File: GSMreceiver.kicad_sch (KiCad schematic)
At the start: 6 parts

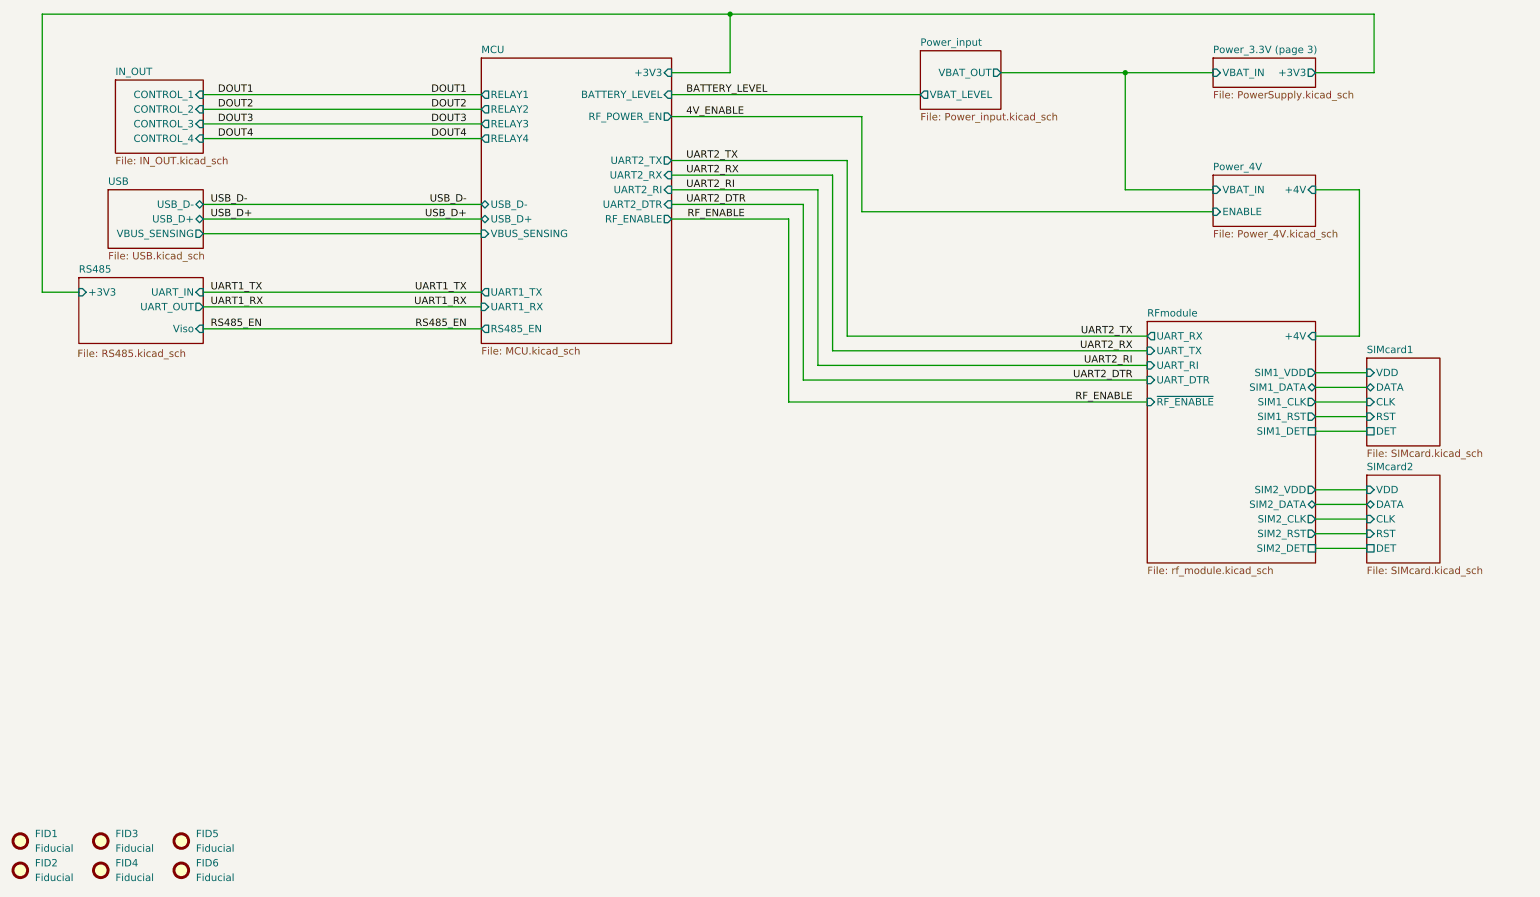
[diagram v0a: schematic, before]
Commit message: Replace SIM800C-DS with A7682E
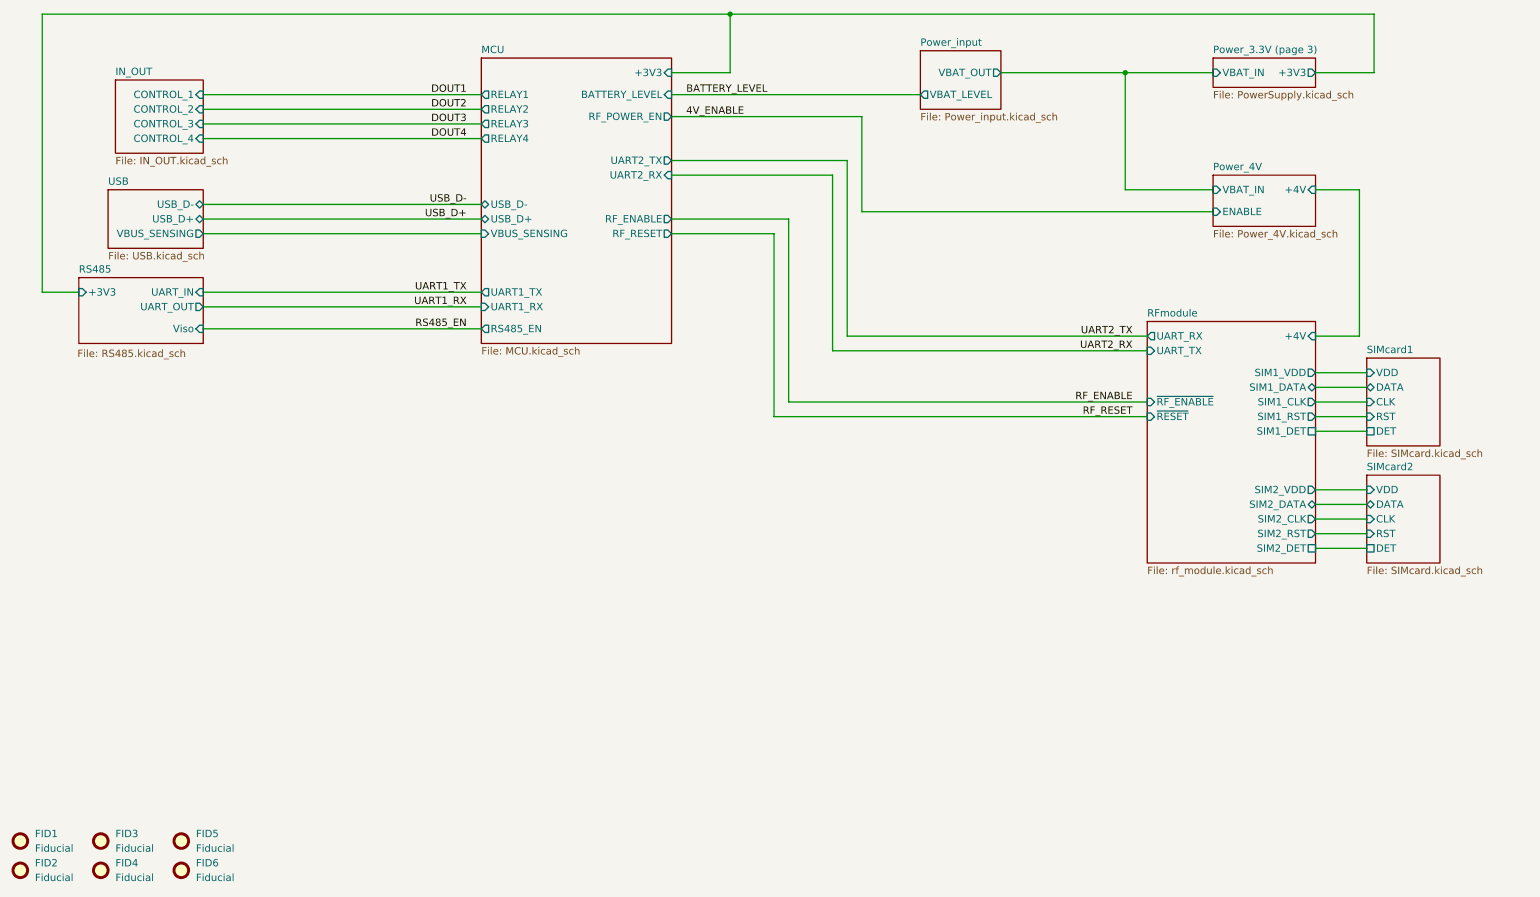
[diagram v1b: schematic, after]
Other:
- sheet MCU ports: added RF_RESET; removed UART2_DTR, UART2_RI
- sheet RFmodule ports: added ~{RESET}; removed UART_DTR, UART_RI
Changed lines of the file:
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@@
+	(wire
+		(pts
+			(xy 148.59 113.03) (xy 213.36 113.03)
+		)
+		(stroke
+			(width 0)
+			(type default)
+		)
+	)
 	(wire
 		(pts
@@
 	(wire
 		(pts
-			(xy 156.21 73.66) (xy 156.21 104.14)
-		)
-		(stroke
-			(width 0)
-			(type default)
-		)
-	)
-	(wire
-		(pts
 			(xy 49.53 59.69) (xy 97.79 59.69)
 		)
@@
 	(wire
 		(pts
+			(xy 130.81 81.28) (xy 148.59 81.28)
+		)
+		(stroke
+			(width 0)
+			(type default)
+		)
+	)
+	(wire
+		(pts
 			(xy 49.53 97.79) (xy 97.79 97.79)
 		)
@@
 	(wire
 		(pts
-			(xy 153.67 106.68) (xy 213.36 106.68)
-		)
-		(stroke
-			(width 0)
-			(type default)
-		)
-	)
-	(wire
-		(pts
 			(xy 224.79 73.66) (xy 209.55 73.66)
 		)
@@
 	(wire
 		(pts
-			(xy 130.81 73.66) (xy 156.21 73.66)
-		)
-		(stroke
-			(width 0)
-			(type default)
-		)
-	)
-	(wire
-		(pts
 			(xy 140.97 43.18) (xy 140.97 53.34)
 		)
@@
 	(wire
 		(pts
+			(xy 148.59 81.28) (xy 148.59 113.03)
+		)
+		(stroke
+			(width 0)
+			(type default)
+		)
+	)
+	(wire
+		(pts
 			(xy 130.81 57.15) (xy 173.99 57.15)
 		)
@@
 	(wire
 		(pts
-			(xy 156.21 104.14) (xy 213.36 104.14)
-		)
-		(stroke
-			(width 0)
-			(type default)
-		)
-	)
-	(wire
-		(pts
 			(xy 161.29 68.58) (xy 161.29 99.06)
 		)
@@
 	(wire
 		(pts
-			(xy 153.67 76.2) (xy 153.67 106.68)
-		)
-		(stroke
-			(width 0)
-			(type default)
-		)
-	)
-	(wire
-		(pts
 			(xy 151.13 78.74) (xy 151.13 110.49)
 		)
@@
 		(pts
 			(xy 242.57 53.34) (xy 252.73 53.34)
-		)
-		(stroke
-			(width 0)
-			(type default)
-		)
-	)
-	(wire
-		(pts
-			(xy 130.81 76.2) (xy 153.67 76.2)
 		)
 		(stroke
@@
 		)
 	)
-	(label "UART1_RX"
-		(at 50.8 93.98 0)
-		(effects
-			(font
-				(size 1.27 1.27)
-			)
-			(justify left bottom)
-		)
-	)
 	(label "UART1_TX"
 		(at 95.25 91.44 180)
@@
 		)
 	)
-	(label "DOUT3"
-		(at 52.07 62.23 0)
-		(effects
-			(font
-				(size 1.27 1.27)
-			)
-			(justify left bottom)
-		)
-	)
 	(label "DOUT1"
 		(at 95.25 57.15 180)
@@
 		)
 	)
-	(label "USB_D-"
-		(at 50.8 76.2 0)
-		(effects
-			(font
-				(size 1.27 1.27)
-			)
-			(justify left bottom)
-		)
-	)
 	(label "RS485_EN"
 		(at 95.25 97.79 180)
@@
 		)
 	)
-	(label "UART2_RI"
-		(at 210.82 104.14 180)
-		(effects
-			(font
-				(size 1.27 1.27)
-			)
-			(justify right bottom)
-		)
-	)
-	(label "UART2_RI"
-		(at 133.35 73.66 0)
-		(effects
-			(font
-				(size 1.27 1.27)
-			)
-			(justify left bottom)
-		)
-	)
-	(label "UART2_DTR"
-		(at 133.35 76.2 0)
-		(effects
-			(font
-				(size 1.27 1.27)
-			)
-			(justify left bottom)
-		)
-	)
-	(label "UART2_TX"
-		(at 133.35 68.58 0)
-		(effects
-			(font
-				(size 1.27 1.27)
-			)
-			(justify left bottom)
-		)
-	)
-	(label "RS485_EN"
-		(at 50.8 97.79 0)
-		(effects
-			(font
-				(size 1.27 1.27)
-			)
-			(justify left bottom)
-		)
-	)
-	(label "DOUT1"
-		(at 52.07 57.15 0)
-		(effects
-			(font
-				(size 1.27 1.27)
-			)
-			(justify left bottom)
-		)
-	)
-	(label "USB_D+"
-		(at 50.8 78.74 0)
-		(effects
-			(font
-				(size 1.27 1.27)
-			)
-			(justify left bottom)
-		)
-	)
-	(label "RF_ENABLE"
-		(at 143.51 78.74 180)
-		(effects
-			(font
-				(size 1.27 1.27)
-			)
-			(justify right bottom)
-		)
-	)
 	(label "USB_D+"
 		(at 95.25 78.74 180)
@@
 		)
 	)
-	(label "UART2_DTR"
-		(at 210.82 106.68 180)
-		(effects
-			(font
-				(size 1.27 1.27)
-			)
-			(justify right bottom)
-		)
-	)
-	(label "DOUT2"
-		(at 52.07 59.69 0)
-		(effects
-			(font
-				(size 1.27 1.27)
-			)
-			(justify left bottom)
-		)
-	)
-	(label "UART1_TX"
-		(at 50.8 91.44 0)
-		(effects
-			(font
-				(size 1.27 1.27)
-			)
-			(justify left bottom)
-		)
-	)
 	(label "DOUT2"
 		(at 95.25 59.69 180)
@@
 		)
 	)
-	(label "UART2_RX"
-		(at 133.35 71.12 0)
+	(label "RF_RESET"
+		(at 210.82 113.03 180)
 		(effects
 			(font
 				(size 1.27 1.27)
 			)
-			(justify left bottom)
+			(justify right bottom)
 		)
 	)
@@
 			)
 			(justify right bottom)
-		)
-	)
-	(label "DOUT4"
-		(at 52.07 64.77 0)
-		(effects
-			(font
-				(size 1.27 1.27)
-			)
-			(justify left bottom)
 		)
 	)
@@
 			)
 		)
-		(pin "UART_DTR" input
-			(at 213.36 106.68 180)
-			(effects
-				(font
-					(size 1.27 1.27)
-				)
-				(justify left)
-			)
-		)
 		(pin "SIM1_CLK" output
 			(at 242.57 110.49 0)
@@
 			)
 		)
-		(pin "UART_RI" input
-			(at 213.36 104.14 180)
-			(effects
-				(font
-					(size 1.27 1.27)
-				)
-				(justify left)
-			)
-		)
 		(pin "UART_RX" output
 			(at 213.36 99.06 180)
@@
 		(pin "UART_TX" input
 			(at 213.36 101.6 180)
+			(effects
+				(font
+					(size 1.27 1.27)
+				)
+				(justify left)
+			)
+		)
+		(pin "~{RESET}" input
+			(at 213.36 113.03 180)
 			(effects
 				(font
@@
 			)
 		)
-		(pin "UART2_DTR" input
-			(at 130.81 76.2 0)
-			(effects
-				(font
-					(size 1.27 1.27)
-				)
-				(justify right)
-			)
-		)
-		(pin "UART2_RI" input
-			(at 130.81 73.66 0)
-			(effects
-				(font
-					(size 1.27 1.27)
-				)
-				(justify right)
-			)
-		)
 		(pin "UART2_RX" input
 			(at 130.81 71.12 0)
@@
 			)
 		)
+		(pin "RF_RESET" output
+			(at 130.81 81.28 0)
+			(effects
+				(font
+					(size 1.27 1.27)
+				)
+				(justify right)
+			)
+		)

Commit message: USB connector inversion fix
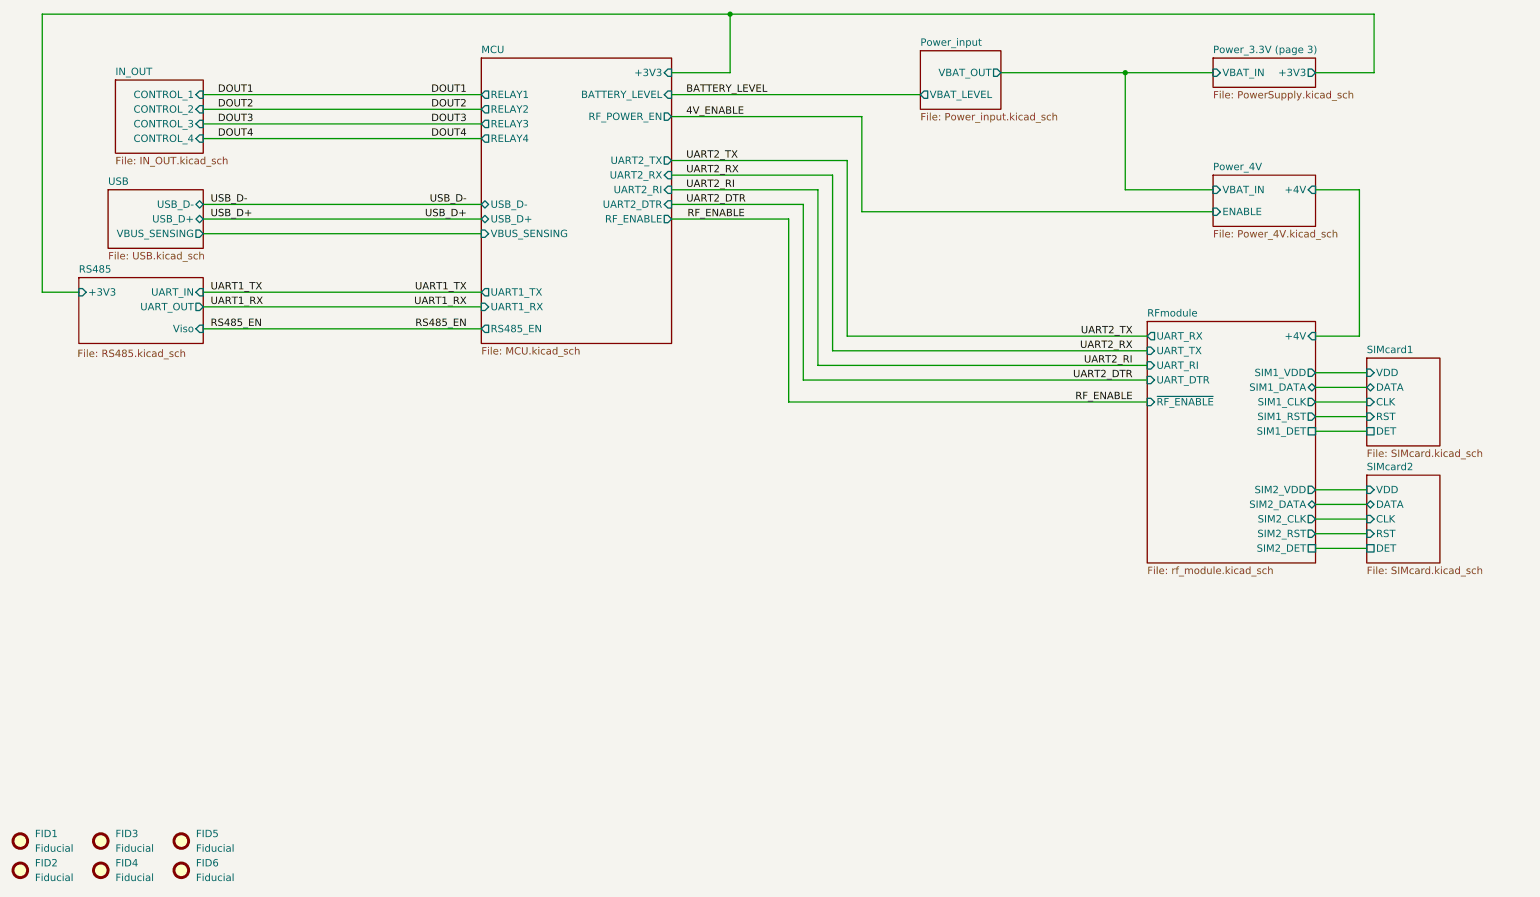
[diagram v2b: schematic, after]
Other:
- sheet MCU ports: added UART2_DTR, UART2_RI; removed RF_RESET
- sheet RFmodule ports: added UART_DTR, UART_RI; removed ~{RESET}
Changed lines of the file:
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@@
-	(wire
-		(pts
-			(xy 148.59 113.03) (xy 213.36 113.03)
-		)
-		(stroke
-			(width 0)
-			(type default)
-		)
-	)
 	(wire
 		(pts
@@
 	(wire
 		(pts
+			(xy 156.21 73.66) (xy 156.21 104.14)
+		)
+		(stroke
+			(width 0)
+			(type default)
+		)
+	)
+	(wire
+		(pts
 			(xy 49.53 59.69) (xy 97.79 59.69)
 		)
@@
 	(wire
 		(pts
-			(xy 130.81 81.28) (xy 148.59 81.28)
-		)
-		(stroke
-			(width 0)
-			(type default)
-		)
-	)
-	(wire
-		(pts
 			(xy 49.53 97.79) (xy 97.79 97.79)
 		)
@@
 	(wire
 		(pts
+			(xy 153.67 106.68) (xy 213.36 106.68)
+		)
+		(stroke
+			(width 0)
+			(type default)
+		)
+	)
+	(wire
+		(pts
 			(xy 224.79 73.66) (xy 209.55 73.66)
 		)
@@
 	(wire
 		(pts
+			(xy 130.81 73.66) (xy 156.21 73.66)
+		)
+		(stroke
+			(width 0)
+			(type default)
+		)
+	)
+	(wire
+		(pts
 			(xy 140.97 43.18) (xy 140.97 53.34)
 		)
@@
 	(wire
 		(pts
-			(xy 148.59 81.28) (xy 148.59 113.03)
-		)
-		(stroke
-			(width 0)
-			(type default)
-		)
-	)
-	(wire
-		(pts
 			(xy 130.81 57.15) (xy 173.99 57.15)
 		)
@@
 	(wire
 		(pts
+			(xy 156.21 104.14) (xy 213.36 104.14)
+		)
+		(stroke
+			(width 0)
+			(type default)
+		)
+	)
+	(wire
+		(pts
 			(xy 161.29 68.58) (xy 161.29 99.06)
 		)
@@
 	(wire
 		(pts
+			(xy 153.67 76.2) (xy 153.67 106.68)
+		)
+		(stroke
+			(width 0)
+			(type default)
+		)
+	)
+	(wire
+		(pts
 			(xy 151.13 78.74) (xy 151.13 110.49)
 		)
@@
 		(pts
 			(xy 242.57 53.34) (xy 252.73 53.34)
+		)
+		(stroke
+			(width 0)
+			(type default)
+		)
+	)
+	(wire
+		(pts
+			(xy 130.81 76.2) (xy 153.67 76.2)
 		)
 		(stroke
@@
 		)
 	)
+	(label "UART1_RX"
+		(at 50.8 93.98 0)
+		(effects
+			(font
+				(size 1.27 1.27)
+			)
+			(justify left bottom)
+		)
+	)
 	(label "UART1_TX"
 		(at 95.25 91.44 180)
@@
 		)
 	)
+	(label "DOUT3"
+		(at 52.07 62.23 0)
+		(effects
+			(font
+				(size 1.27 1.27)
+			)
+			(justify left bottom)
+		)
+	)
 	(label "DOUT1"
 		(at 95.25 57.15 180)
@@
 		)
 	)
+	(label "USB_D-"
+		(at 50.8 76.2 0)
+		(effects
+			(font
+				(size 1.27 1.27)
+			)
+			(justify left bottom)
+		)
+	)
 	(label "RS485_EN"
 		(at 95.25 97.79 180)
@@
 		)
 	)
+	(label "UART2_RI"
+		(at 210.82 104.14 180)
+		(effects
+			(font
+				(size 1.27 1.27)
+			)
+			(justify right bottom)
+		)
+	)
+	(label "UART2_RI"
+		(at 133.35 73.66 0)
+		(effects
+			(font
+				(size 1.27 1.27)
+			)
+			(justify left bottom)
+		)
+	)
+	(label "UART2_DTR"
+		(at 133.35 76.2 0)
+		(effects
+			(font
+				(size 1.27 1.27)
+			)
+			(justify left bottom)
+		)
+	)
+	(label "UART2_TX"
+		(at 133.35 68.58 0)
+		(effects
+			(font
+				(size 1.27 1.27)
+			)
+			(justify left bottom)
+		)
+	)
+	(label "RS485_EN"
+		(at 50.8 97.79 0)
+		(effects
+			(font
+				(size 1.27 1.27)
+			)
+			(justify left bottom)
+		)
+	)
+	(label "DOUT1"
+		(at 52.07 57.15 0)
+		(effects
+			(font
+				(size 1.27 1.27)
+			)
+			(justify left bottom)
+		)
+	)
+	(label "USB_D+"
+		(at 50.8 78.74 0)
+		(effects
+			(font
+				(size 1.27 1.27)
+			)
+			(justify left bottom)
+		)
+	)
+	(label "RF_ENABLE"
+		(at 143.51 78.74 180)
+		(effects
+			(font
+				(size 1.27 1.27)
+			)
+			(justify right bottom)
+		)
+	)
 	(label "USB_D+"
 		(at 95.25 78.74 180)
@@
 		)
 	)
+	(label "UART2_DTR"
+		(at 210.82 106.68 180)
+		(effects
+			(font
+				(size 1.27 1.27)
+			)
+			(justify right bottom)
+		)
+	)
+	(label "DOUT2"
+		(at 52.07 59.69 0)
+		(effects
+			(font
+				(size 1.27 1.27)
+			)
+			(justify left bottom)
+		)
+	)
+	(label "UART1_TX"
+		(at 50.8 91.44 0)
+		(effects
+			(font
+				(size 1.27 1.27)
+			)
+			(justify left bottom)
+		)
+	)
 	(label "DOUT2"
 		(at 95.25 59.69 180)
@@
 		)
 	)
-	(label "RF_RESET"
-		(at 210.82 113.03 180)
-		(effects
-			(font
-				(size 1.27 1.27)
-			)
-			(justify right bottom)
+	(label "UART2_RX"
+		(at 133.35 71.12 0)
+		(effects
+			(font
+				(size 1.27 1.27)
+			)
+			(justify left bottom)
 		)
 	)
@@
 			)
 			(justify right bottom)
+		)
+	)
+	(label "DOUT4"
+		(at 52.07 64.77 0)
+		(effects
+			(font
+				(size 1.27 1.27)
+			)
+			(justify left bottom)
 		)
 	)
@@
 			)
 		)
+		(pin "UART_DTR" input
+			(at 213.36 106.68 180)
+			(effects
+				(font
+					(size 1.27 1.27)
+				)
+				(justify left)
+			)
+		)
 		(pin "SIM1_CLK" output
 			(at 242.57 110.49 0)
@@
 			)
 		)
+		(pin "UART_RI" input
+			(at 213.36 104.14 180)
+			(effects
+				(font
+					(size 1.27 1.27)
+				)
+				(justify left)
+			)
+		)
 		(pin "UART_RX" output
 			(at 213.36 99.06 180)
@@
 		(pin "UART_TX" input
 			(at 213.36 101.6 180)
-			(effects
-				(font
-					(size 1.27 1.27)
-				)
-				(justify left)
-			)
-		)
-		(pin "~{RESET}" input
-			(at 213.36 113.03 180)
 			(effects
 				(font
@@
 			)
 		)
+		(pin "UART2_DTR" input
+			(at 130.81 76.2 0)
+			(effects
+				(font
+					(size 1.27 1.27)
+				)
+				(justify right)
+			)
+		)
+		(pin "UART2_RI" input
+			(at 130.81 73.66 0)
+			(effects
+				(font
+					(size 1.27 1.27)
+				)
+				(justify right)
+			)
+		)
 		(pin "UART2_RX" input
 			(at 130.81 71.12 0)
@@
 			)
 		)
-		(pin "RF_RESET" output
-			(at 130.81 81.28 0)
-			(effects
-				(font
-					(size 1.27 1.27)
-				)
-				(justify right)
-			)
-		)
